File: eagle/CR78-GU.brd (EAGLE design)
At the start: 100.8 x 80.8 mm, 18 parts, among them Q522 2N3904, Q523 2N3904, Q7 2N3904

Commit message: more schemo
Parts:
- added 671, R543: 82k, rcl:0207/7
- added C4, C5: 68n, rcl:C050-025X075
- added D519, D520, D527: (no value), SparkFun-DiscreteSemi:DIODE-1N4148
- added Q520, Q521: 2N3904, 808_lt:TO92
- added R5, R6: 56k, rcl:0207/7
- added R546: 2M2, rcl:0207/7
- added R672: 47k, rcl:0207/7
- added R673: 5k6, rcl:0207/7
- added R674: 15k, rcl:0207/7
- added R675: 10k, rcl:0207/7
- added R676: 3k9, rcl:0207/7
- added R677: 18k, rcl:0207/7
- renumbered Q522 to Q518, Q523 to Q519, R551 to R667, R552 to R668, R553 to R669, R554 to R670
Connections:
- new net N$1: 671.2, D519.C, R677.2
- new net N$10: R673.1, R674.1, R675.1, R676.2
- new net N$12: R676.1, VR59.E, VR59.S
- new net N$14: R6.1, VR59.A
- new net N$2: C5.1, D519.A, Q520.2, R543.2
- new net N$22: R5.1, R543.1, R6.2, R672.2
- new net N$23: D527.C, R672.1
- new net N$4: Q520.3, Q521.3
- new net N$5: D520.C, Q521.1, R546.2, R675.2
- new net N$6: C5.2, D520.A, R674.2
- new net N$8: C4.2, Q521.2, R5.2
- new net N$9: C4.1, Q520.1, R673.2
- net GND: now also R677.1
- net N$20: now also 671.1
- net N$46: now also D527.A

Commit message: schemo in
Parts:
- added C507: 100/10, rcl:B45181A
- added C531: 22n, rcl:C050-025X075
- added C532: 15n, rcl:C050-025X075
- added L4: 45mH, rcl:0204/7
- added Q508: 2N3904, 808_lt:TO92
- added R547: 47k, rcl:0207/7
- added R548: 470k, rcl:0207/7
- added R549: 10k, rcl:0207/7
- added R550: 820, rcl:0207/7
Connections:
- new net N$13: Q508.2, R547.2, R548.2
- new net N$27: C1.1, C532.2, L4.2, Q508.1
- net +12V: now also C532.1, L4.1, R549.1, R676.1, VR59.E, VR59.S
- net GND: now also C507.-, R550.2
- net N$12: now also C531.1, R546.1, R547.1; no longer R676.1, VR59.E, VR59.S
- net N$26: now also C531.2
- net N$4: now also C507.+, Q508.3, R548.1, R549.2, R550.1
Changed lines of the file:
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@@
 <element name="R672" library="rcl" package="0207/7" value="47k" x="-11.43" y="-101.6"/>
 <element name="R6" library="rcl" package="0207/7" value="56k" x="-11.43" y="-106.68"/>
+<element name="R547" library="rcl" package="0207/7" value="47k" x="-11.43" y="-111.76"/>
+<element name="Q508" library="808_lt" package="TO92" value="2N3904" x="-12.7" y="-116.84"/>
+<element name="R548" library="rcl" package="0207/7" value="470k" x="-11.43" y="-121.92"/>
+<element name="C507" library="rcl" package="B45181A" value="100/10" x="-12.7" y="-128.27"/>
+<element name="C532" library="rcl" package="C050-025X075" value="15n" x="-11.43" y="-134.62"/>
+<element name="R549" library="rcl" package="0207/7" value="10k" x="-11.43" y="-142.24"/>
+<element name="L4" library="rcl" package="0204/7" value="45mH" x="-11.43" y="-147.32"/>
+<element name="R550" library="rcl" package="0207/7" value="820" x="-11.43" y="-152.4"/>
+<element name="C531" library="rcl" package="C050-025X075" value="22n" x="-11.43" y="-157.48"/>
 </elements>
 <signals>
@@
 <wire x1="42.926" y1="16.1925" x2="42.9895" y2="16.256" width="0.8128" layer="16"/>
 <contactref element="GU" pad="4"/>
-<wire x1="11.684" y1="37.338" x2="11.938" y2="37.338" width="0" layer="19" extent="16-16"/>
+<contactref element="R676" pad="1"/>
+<contactref element="VR59" pad="E"/>
+<contactref element="VR59" pad="S"/>
+<contactref element="L4" pad="1"/>
+<contactref element="C532" pad="1"/>
+<contactref element="R549" pad="1"/>
+<wire x1="-15.24" y1="-142.24" x2="-15.24" y2="-147.32" width="0" layer="19" extent="1-1"/>
+<wire x1="-13.97" y1="-134.62" x2="-15.24" y2="-142.24" width="0" layer="19" extent="1-1"/>
+<wire x1="-15.24" y1="-87.63" x2="-13.97" y2="-134.62" width="0" layer="19" extent="1-1"/>
+<wire x1="-6.35" y1="-10.16" x2="-15.24" y2="-87.63" width="0" layer="19" extent="1-1"/>
+<wire x1="-12.7" y1="1.27" x2="-6.35" y2="-10.16" width="0" layer="19" extent="1-1"/>
+<wire x1="-15.24" y1="1.27" x2="-12.7" y2="1.27" width="0" layer="19" extent="1-1"/>
+<wire x1="11.684" y1="37.338" x2="-12.7" y2="1.27" width="0" layer="19" extent="1-1"/>
+<wire x1="11.938" y1="37.338" x2="11.684" y2="37.338" width="0" layer="19" extent="16-16"/>
 <wire x1="25.8445" y1="39.9415" x2="23.495" y2="37.973" width="0" layer="19" extent="16-16"/>
-<wire x1="-6.35" y1="-10.16" x2="35.052" y2="9.144" width="0" layer="19" extent="1-1"/>
 </signal>
 <signal name="GND">
@@
 <contactref element="GU" pad="5"/>
 <contactref element="R677" pad="1"/>
-<wire x1="21.844" y1="26.924" x2="31.496" y2="34.036" width="0" layer="19" extent="16-16"/>
+<contactref element="C507" pad="-"/>
+<contactref element="R550" pad="2"/>
+<wire x1="-11.43" y1="-128.27" x2="-7.62" y2="-152.4" width="0" layer="19" extent="1-1"/>
+<wire x1="-15.24" y1="-22.86" x2="-11.43" y2="-128.27" width="0" layer="19" extent="1-1"/>
+<wire x1="-3.81" y1="-10.16" x2="-15.24" y2="-22.86" width="0" layer="19" extent="1-1"/>
+<wire x1="2.5" y1="7.032" x2="-3.81" y2="-10.16" width="0" layer="19" extent="1-1"/>
+<wire x1="31.496" y1="34.036" x2="21.844" y2="26.924" width="0" layer="19" extent="16-16"/>
 <wire x1="21.082" y1="11.557" x2="21.844" y2="26.924" width="0" layer="19" extent="16-16"/>
-<wire x1="-3.81" y1="-10.16" x2="2.5" y2="7.032" width="0" layer="19" extent="1-1"/>
-<wire x1="-15.24" y1="-22.86" x2="-3.81" y2="-10.16" width="0" layer="19" extent="1-1"/>
 </signal>
 <signal name="N$46">
@@
 <signal name="N$26">
 <contactref element="VR63" pad="A"/>
+<contactref element="C531" pad="2"/>
+<wire x1="25.654" y1="40.132" x2="-8.89" y2="-157.48" width="0" layer="19" extent="1-1"/>
 </signal>
 <signal name="N$1">
@@
 <contactref element="Q520" pad="3"/>
 <contactref element="Q521" pad="3"/>
+<contactref element="R548" pad="1"/>
+<contactref element="C507" pad="+"/>
+<contactref element="Q508" pad="3"/>
+<contactref element="R550" pad="1"/>
+<contactref element="R549" pad="2"/>
+<wire x1="-7.62" y1="-142.24" x2="-15.24" y2="-152.4" width="0" layer="19" extent="1-1"/>
+<wire x1="-13.97" y1="-128.27" x2="-7.62" y2="-142.24" width="0" layer="19" extent="1-1"/>
+<wire x1="-15.24" y1="-121.92" x2="-13.97" y2="-128.27" width="0" layer="19" extent="1-1"/>
+<wire x1="-13.97" y1="-116.84" x2="-15.24" y2="-121.92" width="0" layer="19" extent="1-1"/>
+<wire x1="-13.97" y1="-36.83" x2="-13.97" y2="-116.84" width="0" layer="19" extent="1-1"/>
 <wire x1="-13.97" y1="-31.75" x2="-13.97" y2="-36.83" width="0" layer="19" extent="1-1"/>
 </signal>
@@
 <wire x1="-15.24" y1="-62.23" x2="-15.24" y2="-67.31" width="0" layer="19" extent="1-1"/>
 </signal>
-<signal name="N$12">
-<contactref element="R676" pad="1"/>
-<contactref element="VR59" pad="E"/>
-<contactref element="VR59" pad="S"/>
-<wire x1="-15.24" y1="1.27" x2="-15.24" y2="-87.63" width="0" layer="19" extent="1-1"/>
-<wire x1="-12.7" y1="1.27" x2="-15.24" y2="1.27" width="0" layer="19" extent="1-1"/>
-</signal>
 <signal name="N$14">
 <contactref element="VR59" pad="A"/>
@@
 <wire x1="-7.62" y1="-96.52" x2="-15.24" y2="-101.6" width="0" layer="19" extent="1-1"/>
 </signal>
+<signal name="N$12">
+<contactref element="R546" pad="1"/>
+<contactref element="C531" pad="1"/>
+<contactref element="R547" pad="1"/>
+<wire x1="-15.24" y1="-111.76" x2="-13.97" y2="-157.48" width="0" layer="19" extent="1-1"/>
+<wire x1="-15.24" y1="-92.71" x2="-15.24" y2="-111.76" width="0" layer="19" extent="1-1"/>
+</signal>
+<signal name="N$13">
+<contactref element="R547" pad="2"/>
+<contactref element="Q508" pad="2"/>
+<contactref element="R548" pad="2"/>
+<wire x1="-12.7" y1="-114.935" x2="-7.62" y2="-121.92" width="0" layer="19" extent="1-1"/>
+<wire x1="-7.62" y1="-111.76" x2="-12.7" y2="-114.935" width="0" layer="19" extent="1-1"/>
+</signal>
+<signal name="N$27">
+<contactref element="Q508" pad="1"/>
+<contactref element="L4" pad="2"/>
+<contactref element="C532" pad="2"/>
+<contactref element="C1" pad="1"/>
+<wire x1="-8.89" y1="-134.62" x2="-7.62" y2="-147.32" width="0" layer="19" extent="1-1"/>
+<wire x1="-11.43" y1="-116.84" x2="-8.89" y2="-134.62" width="0" layer="19" extent="1-1"/>
+<wire x1="37.846" y1="16.256" x2="-11.43" y2="-116.84" width="0" layer="19" extent="1-1"/>
+</signal>
 </signals>

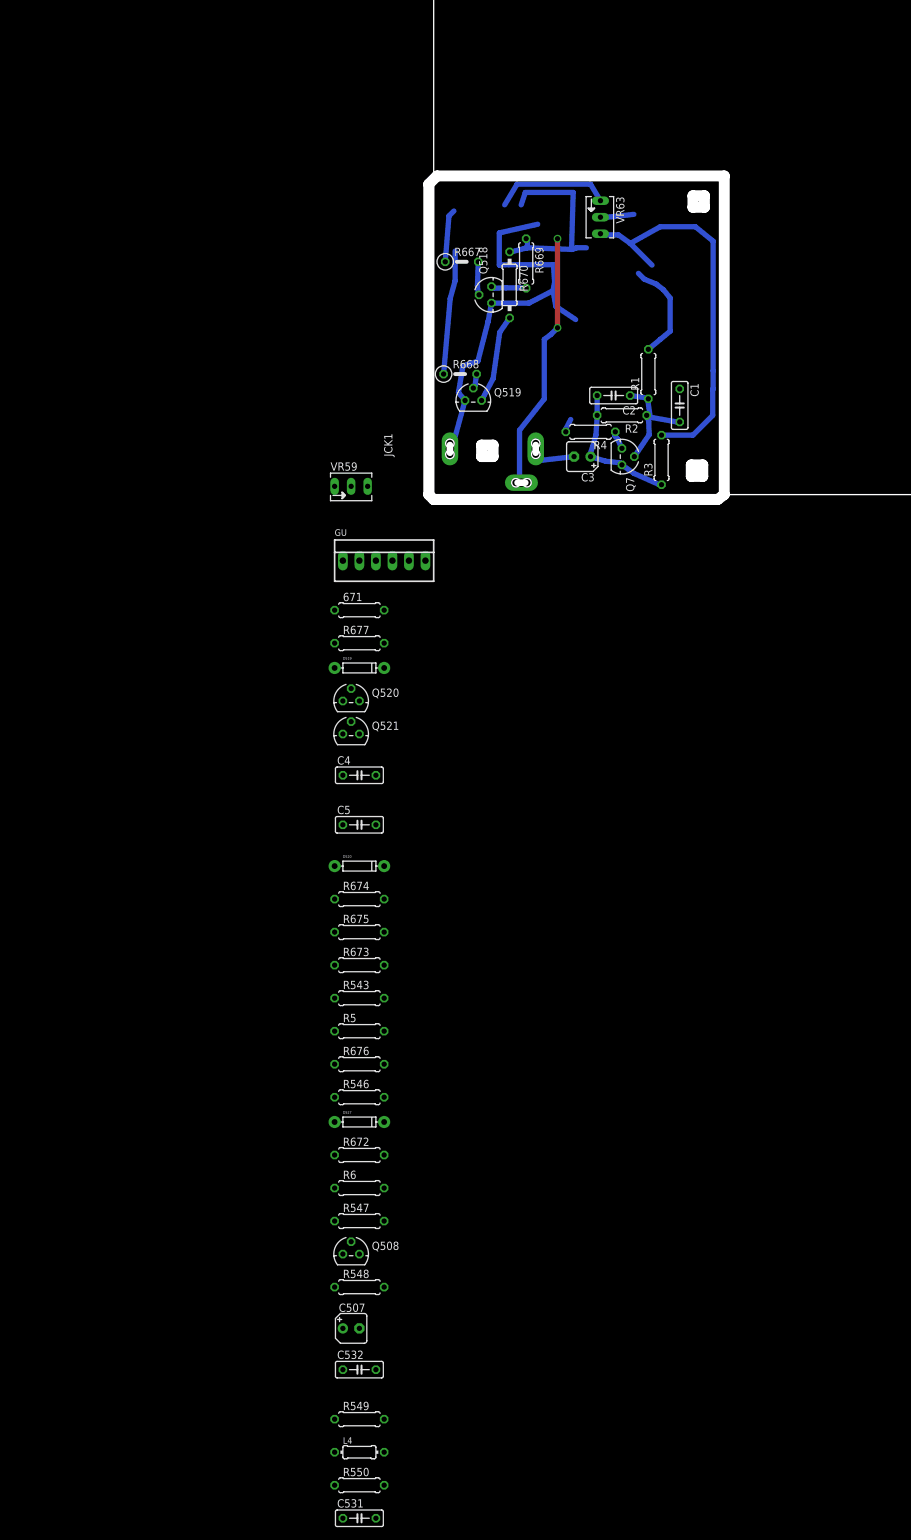
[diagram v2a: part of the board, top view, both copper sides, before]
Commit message: fixed noise input and started board
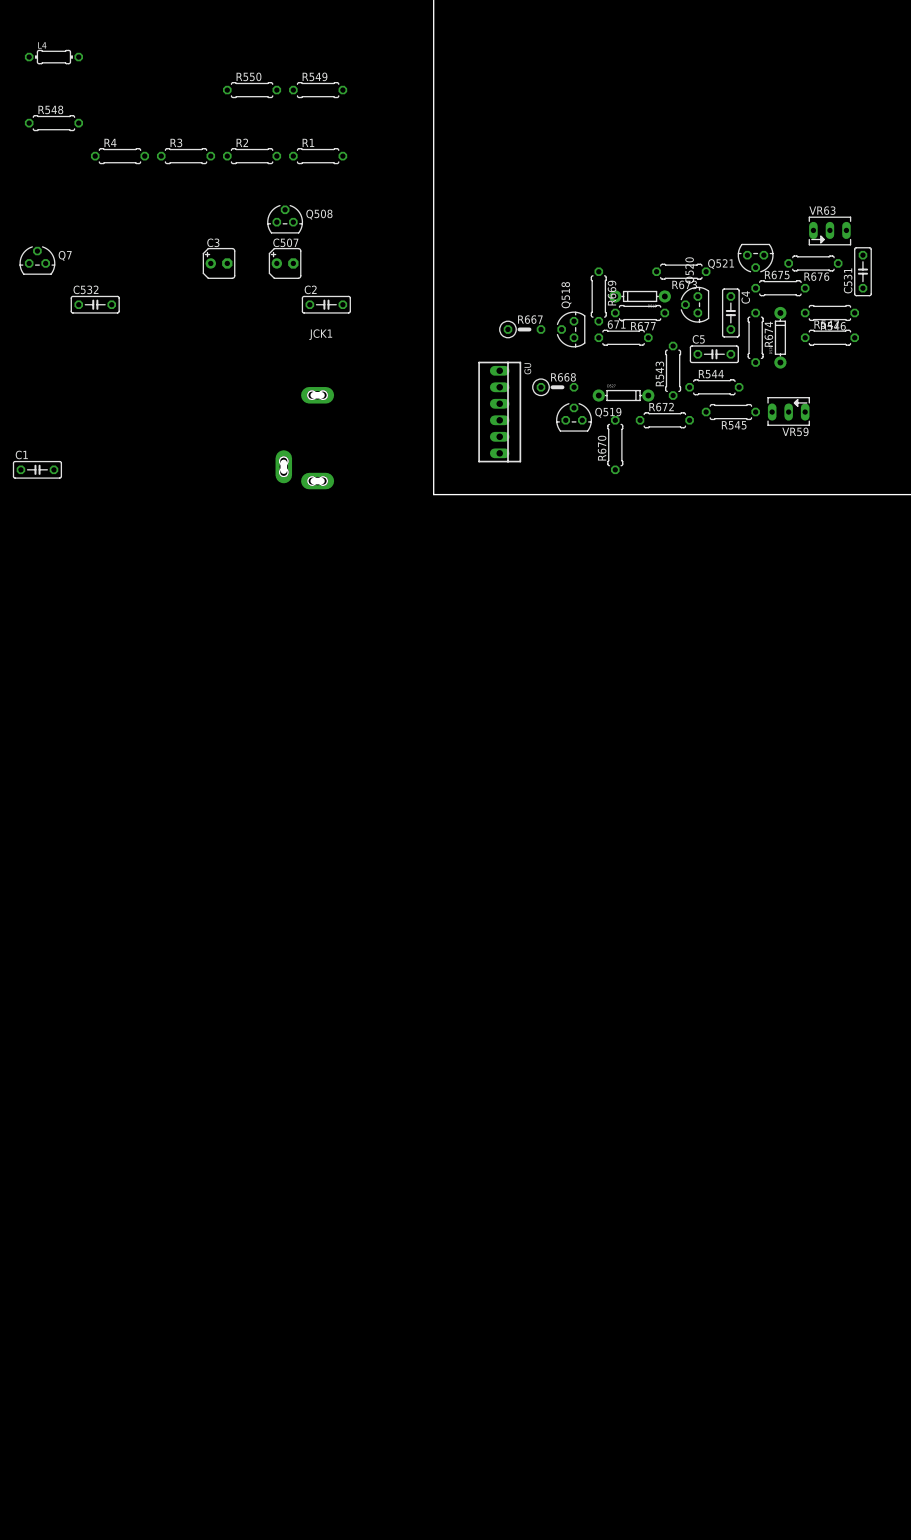
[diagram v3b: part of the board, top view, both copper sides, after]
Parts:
- removed R5, R6: 56k, rcl:0207/7
- added R544, R545: 56k, rcl:0207/7
- R670: device rcl:0207/10 -> rcl:0207/7
- moved L4 219.7 mm to (-58.4, 67.3)
- moved R550 215.3 mm to (-27.9, 62.2)
- moved C531 206.8 mm to (66.0, 34.3), turned to 90 degrees
- moved R549 204.6 mm to (-17.8, 62.2)
- moved R548 185.1 mm to (-58.4, 57.1)
- moved C532 168.8 mm to (-52.1, 29.2)
- moved C507 164.1 mm to (-22.9, 35.6)
- moved Q508 159.1 mm to (-22.9, 41.9)
- moved R547 154.0 mm to (61.0, 24.1)
- moved R676 141.6 mm to (58.4, 35.6), turned to 180 degrees
- moved R546 140.7 mm to (61.0, 27.9), turned to 180 degrees
- moved R672 122.4 mm to (35.6, 11.4)
- moved D527 118.9 mm to (29.2, 15.2)
- moved R675 118.4 mm to (53.3, 31.8)
- moved R673 117.6 mm to (38.1, 34.3), turned to 180 degrees
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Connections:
- removed net N$26: C531.2, VR63.A
- net +12V: now also VR63.A
- net N$14: now also R545.1; no longer R6.1
- net N$17: now also C531.2
- net N$22: now also R544.1, R545.2; no longer R5.1, R6.2
- net N$8: now also R544.2; no longer R5.2
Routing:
- net +12V: track 91.0 -> 0.00 mm
- net GND: track 82.6 -> 0.00 mm
- net N$7: track 39.8 -> 0.00 mm, vias 2 -> 0
- net N$16: track 21.8 -> 0.00 mm
- net N$11: track 19.1 -> 0.00 mm
- net N$18: track 18.5 -> 0.00 mm
- net N$3: track 18.0 -> 0.00 mm
- net N$46: track 13.7 -> 0.00 mm
- net N$24: track 8.15 -> 0.00 mm
- net N$19: track 7.18 -> 0.00 mm
- net N$20: track 5.43 -> 0.00 mm
- net N$17: track 5.18 -> 0.00 mm
- net N$21: track 5.14 -> 0.00 mm
- net N$15: track 2.85 -> 0.00 mm
- net N$47: track 2.25 -> 0.00 mm
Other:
- board size 100.8 x 80.8 mm -> 100 x 80 mm

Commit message: parts on board
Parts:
- moved L4 141.6 mm to (71.1, 10.2), turned to 90 degrees
- moved Q7 136.1 mm to (74.9, 27.9), turned to 90 degrees
- moved C1 134.4 mm to (72.4, 20.3), turned to 90 degrees
- moved R548 131.0 mm to (69.8, 30.5), turned to 270 degrees
- moved R4 128.4 mm to (76.2, 20.3), turned to 270 degrees
- moved C3 120.9 mm to (87.6, 27.9), turned to 270 degrees
- moved JCK1 119.4 mm to (96.5, 15.2), turned to 270 degrees
- moved C532 119.3 mm to (66.0, 12.7), turned to 90 degrees
- moved R3 115.5 mm to (76.2, 35.6), turned to 180 degrees
- moved R2 107.1 mm to (77.5, 33.0)
- moved R1 105.7 mm to (83.8, 22.9)
- moved C2 97.8 mm to (81.3, 29.2)
- moved R550 97.7 mm to (59.7, 19.1), turned to 180 degrees
- moved R549 94.1 mm to (62.2, 12.7), turned to 90 degrees
- moved Q508 92.4 mm to (67.3, 21.6)
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
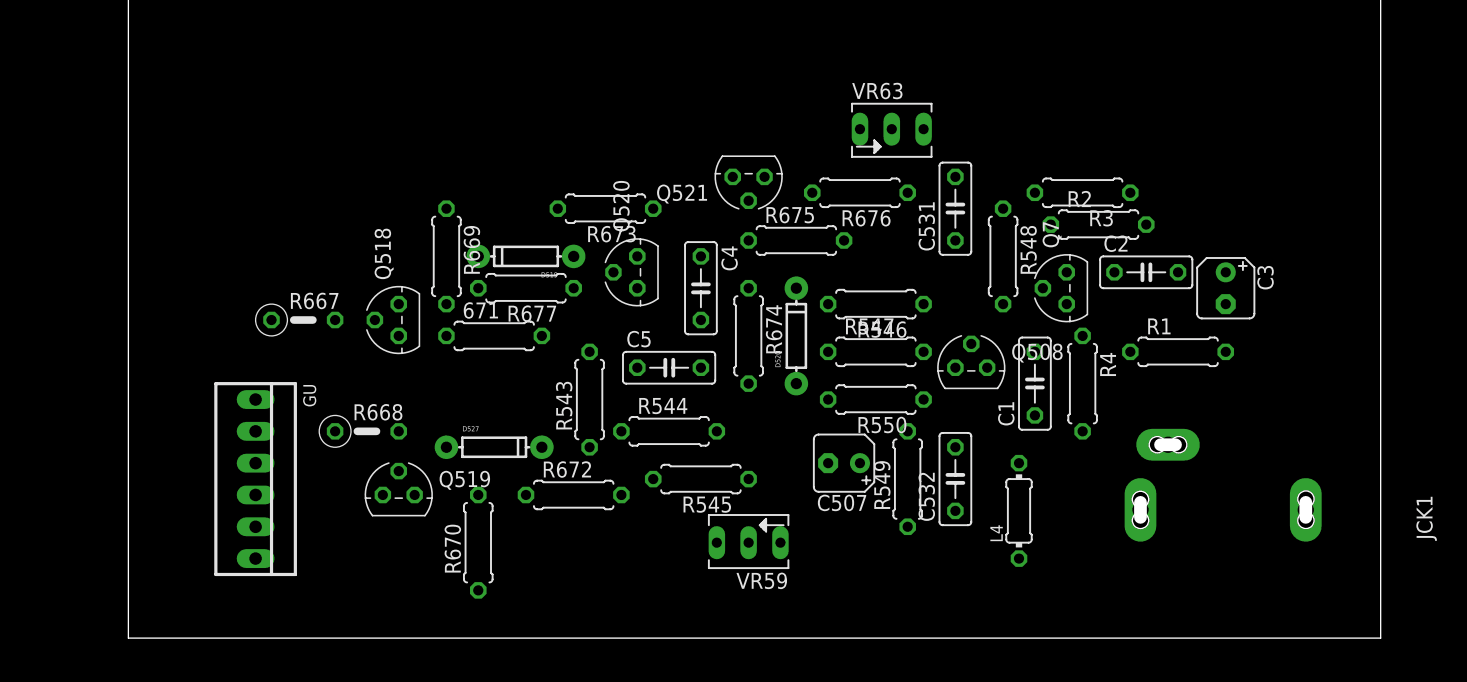
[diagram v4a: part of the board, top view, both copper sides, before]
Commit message: routed with cutout
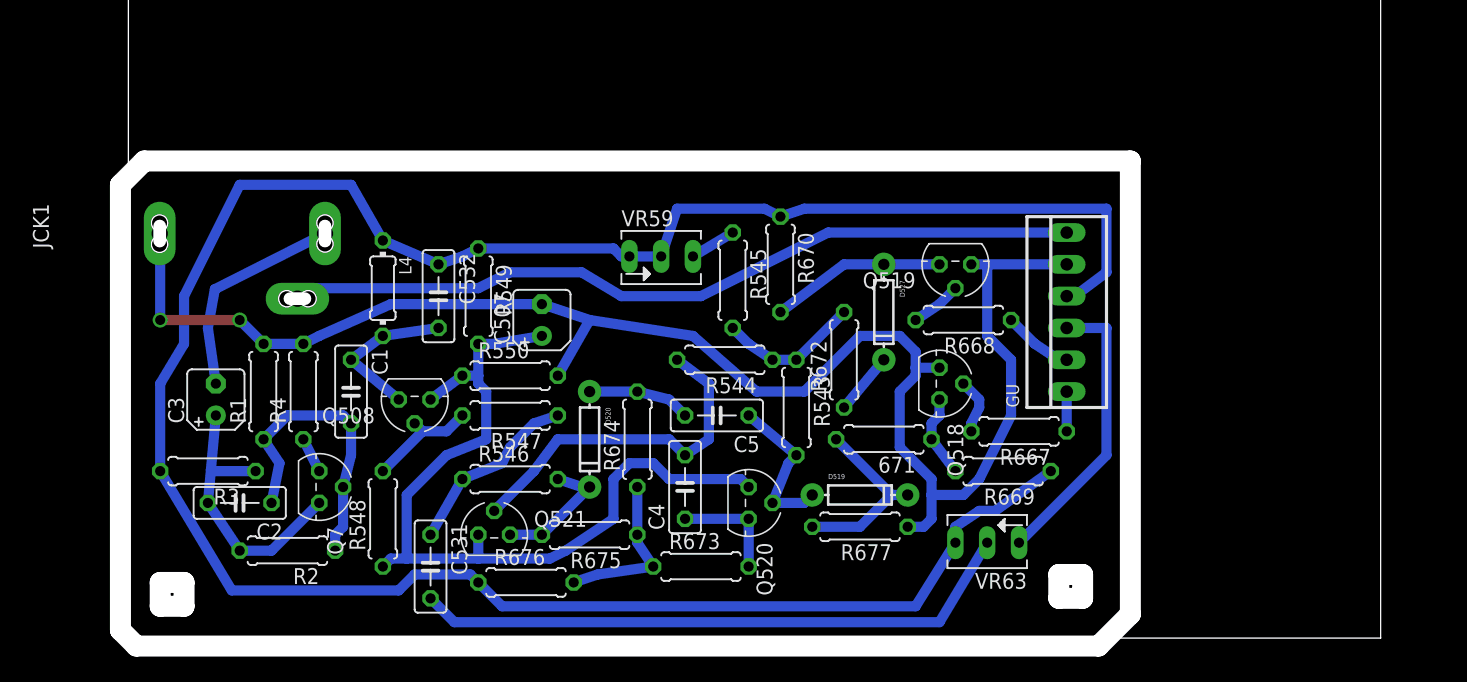
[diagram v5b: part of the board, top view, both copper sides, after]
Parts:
- R667, R668: device rcl:0207/5V -> rcl:0207/7
- moved JCK1 97.3 mm to (0.00, 27.3), turned to 90 degrees
- moved C3 81.1 mm to (6.99, 19.1), turned to 90 degrees
- moved C2 74.7 mm to (8.89, 10.8), turned to 180 degrees
- moved R3 73.3 mm to (6.35, 13.3)
- moved R1 73.1 mm to (10.8, 19.7), turned to 90 degrees
- moved R2 69.8 mm to (12.7, 6.99), turned to 180 degrees
- moved GU 66.1 mm to (74.9, 26.0), turned to 90 degrees
- moved R4 62.2 mm to (14.0, 19.7), turned to 90 degrees
- moved Q7 61.8 mm to (15.2, 12.1), turned to 270 degrees
- moved R667 57.8 mm to (71.1, 16.5), turned to 180 degrees
- moved C1 54.6 mm to (17.8, 19.7), turned to 270 degrees
- moved L4 53.8 mm to (20.3, 27.9), turned to 270 degrees
- moved R548 53.8 mm to (20.3, 9.53), turned to 90 degrees
- moved C531 50.7 mm to (24.1, 5.71), turned to 270 degrees
- moved R668 48.4 mm to (66.7, 25.4), turned to 180 degrees
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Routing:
- net +12V: track 0.00 -> 192.6 mm
- net GND: track 0.00 -> 127.6 mm, vias 0 -> 2
- net N$4: track 0.00 -> 67.2 mm
- net N$7: track 0.00 -> 63.7 mm
- net N$17: track 0.00 -> 48.8 mm
- net N$8: track 0.00 -> 28.3 mm
- net N$18: track 0.00 -> 24.1 mm
- net N$3: track 0.00 -> 23.2 mm
- net N$16: track 0.00 -> 23.1 mm
- net N$19: track 0.00 -> 17.5 mm
- net N$1: track 0.00 -> 15.0 mm
- net N$12: track 0.00 -> 14.7 mm
- net N$46: track 0.00 -> 14.0 mm
- net N$10: track 0.00 -> 13.2 mm
- net N$2: track 0.00 -> 12.7 mm
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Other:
- board size 100 x 80 mm -> 100.6 x 80.6 mm
